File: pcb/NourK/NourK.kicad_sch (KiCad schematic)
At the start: 0 parts

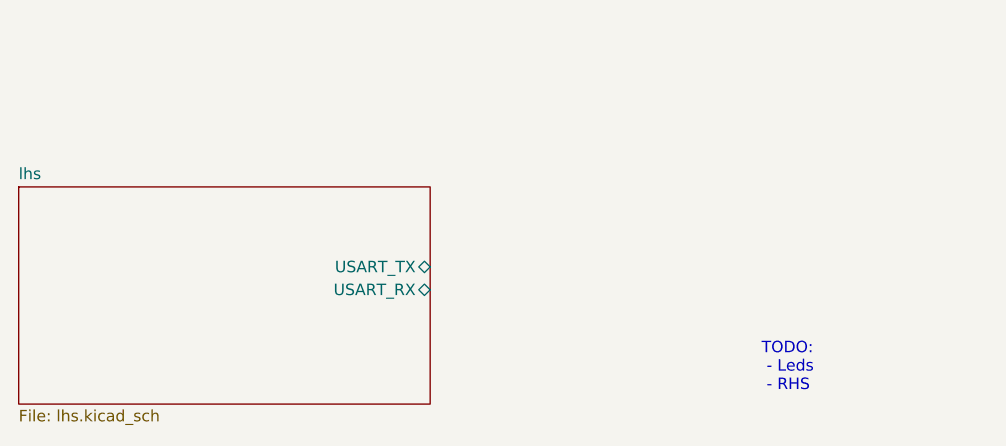
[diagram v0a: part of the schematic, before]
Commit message: Add RHS schematics sheets
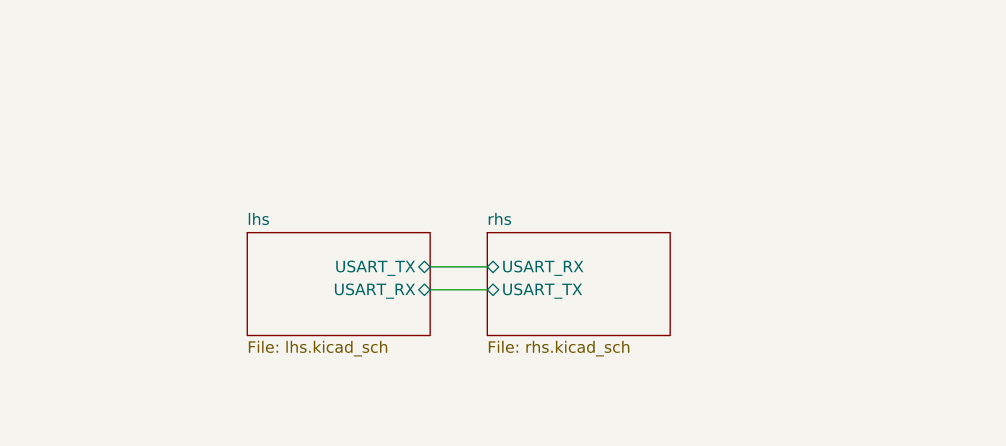
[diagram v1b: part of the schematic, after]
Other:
- added sheet rhs (rhs.kicad_sch)
- note removed: "TODO: - Leds - RHS"

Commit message: Draft LHS tracks
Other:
- sheet lhs ports: added USART{TX RX}; removed USART_RX, USART_TX
- sheet rhs ports: added USART{TX RX}; removed USART_RX, USART_TX

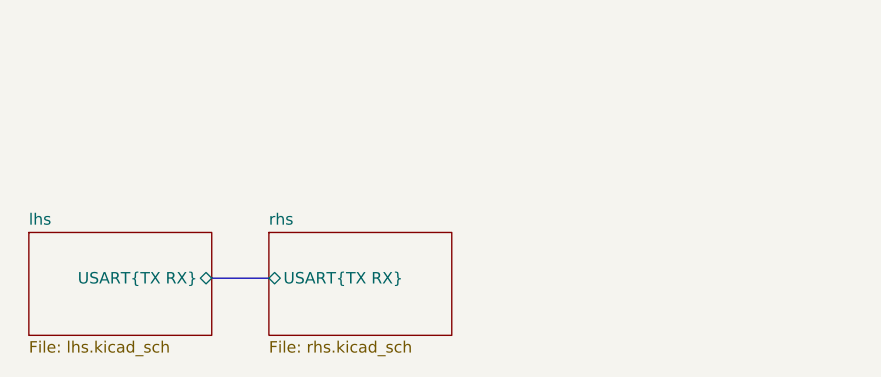
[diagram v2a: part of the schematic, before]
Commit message: Re-traced RHS
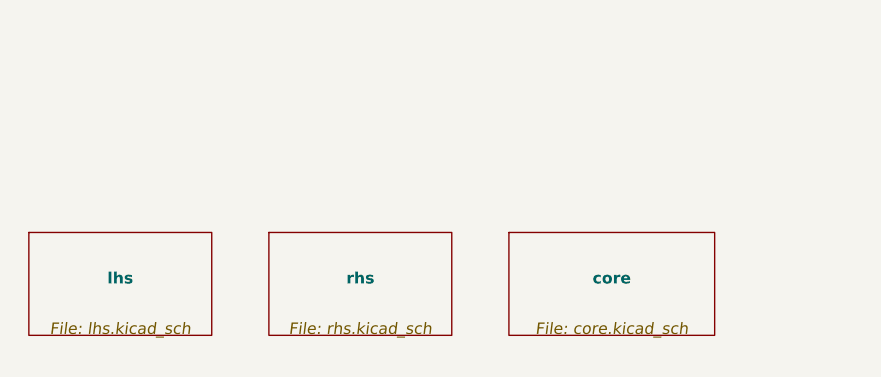
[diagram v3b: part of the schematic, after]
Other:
- added sheet core (core.kicad_sch)
- sheet lhs ports: added none; removed USART{TX RX}
- sheet rhs ports: added none; removed USART{TX RX}

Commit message: Complete wiring
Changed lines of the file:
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@@
     (effects (font (size 1.27 1.27)) (justify left bottom))
-  )
-  (symbol (lib_id "power:VCC") (at 248.92 27.94 0) (unit 1)
-    (in_bom yes) (on_board yes)
-    (property "Reference" "#PWR01" (id 0) (at 248.92 31.75 0)
-      (effects (font (size 1.27 1.27)) hide)
-    )
-    (property "Value" "VCC" (id 1) (at 248.92 24.13 0))
-    (property "Footprint" "" (id 2) (at 248.92 27.94 0)
-      (effects (font (size 1.27 1.27)) hide)
-    )
-    (property "Datasheet" "" (id 3) (at 248.92 27.94 0)
-      (effects (font (size 1.27 1.27)) hide)
-    )
-    (pin "1")
   )
   (symbol (lib_id "power:PWR_FLAG") (at 260.35 27.94 180) (unit 1)
@@
     )
     (property "Datasheet" "" (id 3) (at 260.35 27.94 0)
-      (effects (font (size 1.27 1.27)) hide)
-    )
-    (pin "1")
-  )
-  (symbol (lib_id "power:PWR_FLAG") (at 248.92 27.94 180) (unit 1)
-    (in_bom yes) (on_board yes) (fields_autoplaced)
-    (property "Reference" "#FLG01" (id 0) (at 248.92 29.845 0)
-      (effects (font (size 1.27 1.27)) hide)
-    )
-    (property "Value" "PWR_FLAG" (id 1) (at 248.92 32.3834 0))
-    (property "Footprint" "" (id 2) (at 248.92 27.94 0)
-      (effects (font (size 1.27 1.27)) hide)
-    )
-    (property "Datasheet" "~" (id 3) (at 248.92 27.94 0)
       (effects (font (size 1.27 1.27)) hide)
     )
@@
   )
   (symbol_instances
-    (path "/97725135-a26c-4e56-be6b-8ec2072b85c3"
-      (reference "#FLG01") (unit 1) (value "PWR_FLAG") (footprint "")
-    )
     (path "/3f2a1840-7410-4493-8c9c-528f61d452a1"
       (reference "#FLG02") (unit 1) (value "PWR_FLAG") (footprint "")
@@
       (reference "#FLG0102") (unit 1) (value "PWR_FLAG") (footprint "")
     )
-    (path "/2b25df22-6c20-4b0e-b7d9-ea3f3f376a49"
-      (reference "#PWR01") (unit 1) (value "VCC") (footprint "")
-    )
     (path "/5defae3f-09ec-4a68-b6ca-765f4b4ab3b4"
       (reference "#PWR02") (unit 1) (value "GND") (footprint "")
@@
       (reference "#PWR0138") (unit 1) (value "GND") (footprint "")
     )
-    (path "/a6af0249-c8eb-4b80-99e2-1d85a2fc3025/f25c0cea-84fc-46c9-ba23-36704cb9f78b"
-      (reference "#PWR0139") (unit 1) (value "VCC") (footprint "")
-    )
     (path "/a6af0249-c8eb-4b80-99e2-1d85a2fc3025/a1688a41-d8f5-44d1-8fc7-bd35c079f55e"
